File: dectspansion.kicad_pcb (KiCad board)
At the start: 4 copper layers, 37 x 36.6 mm, 19 parts, among them J1 Hexpansion-Connector, J2 Conn_01x03_Pin, J3 AudioJack4, U2 SC14CVMDECT

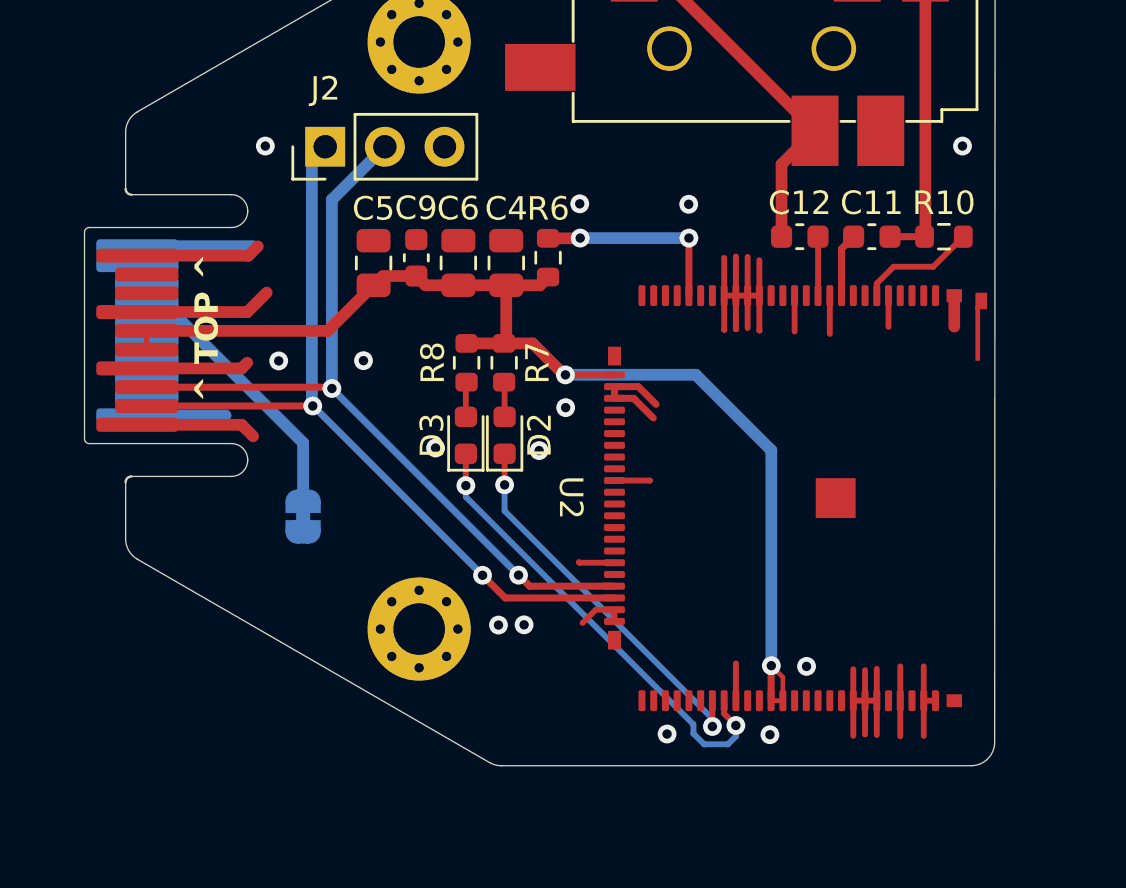
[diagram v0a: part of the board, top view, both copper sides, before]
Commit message: Adjustments to schmatic, board layout, and added part list to readme
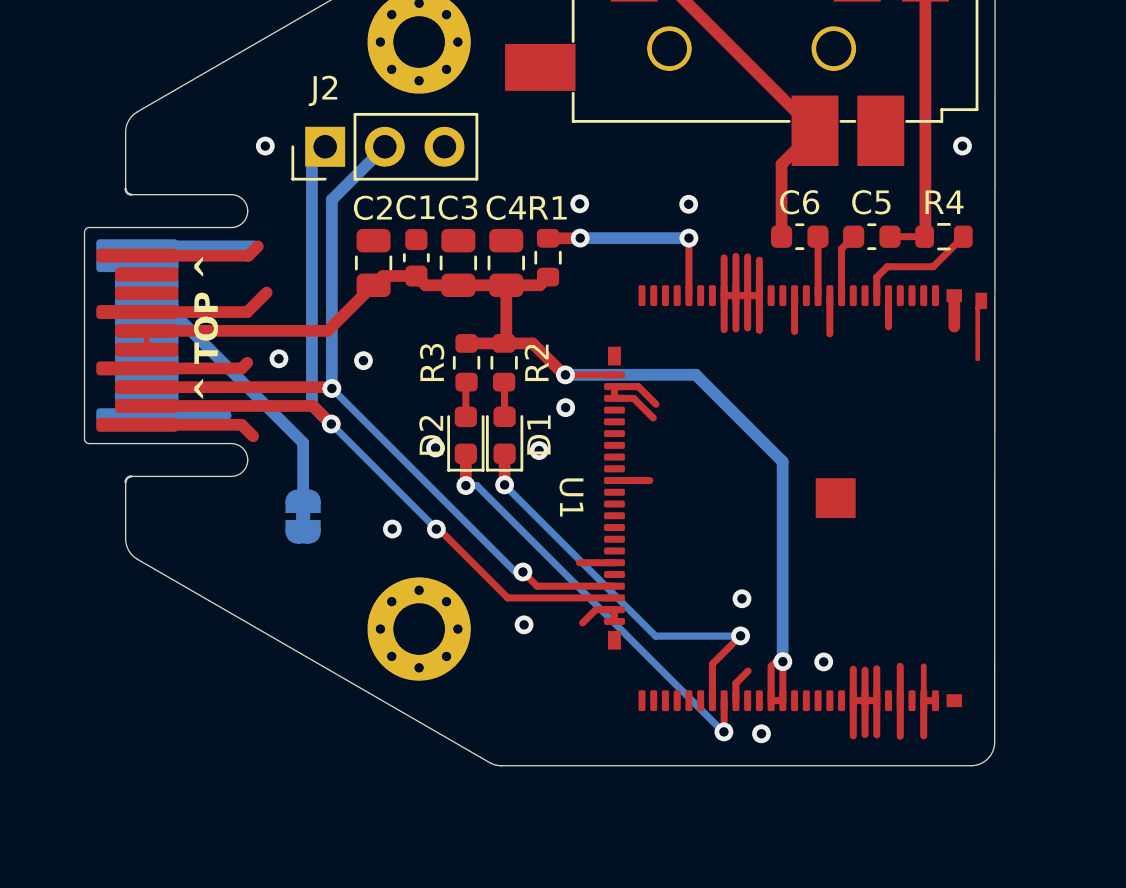
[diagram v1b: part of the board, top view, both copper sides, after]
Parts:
- C5: renamed from C11; value 0U1 -> 0u1
- C6: renamed from C12; value 1N -> 1n
- renumbered C9 to C1, C5 to C2, C6 to C3, D2 to D1, D3 to D2, R6 to R1, R7 to R2, R8 to R3, R10 to R4, U2 to U1
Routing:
- net /HS_I: track 34.6 -> 36.8 mm
- net Net-(D2-K): track 19.8 -> 18.0 mm
- net Net-(D1-K): track 16.8 -> 17.7 mm
- net +3V3: track 51.5 -> 52.1 mm

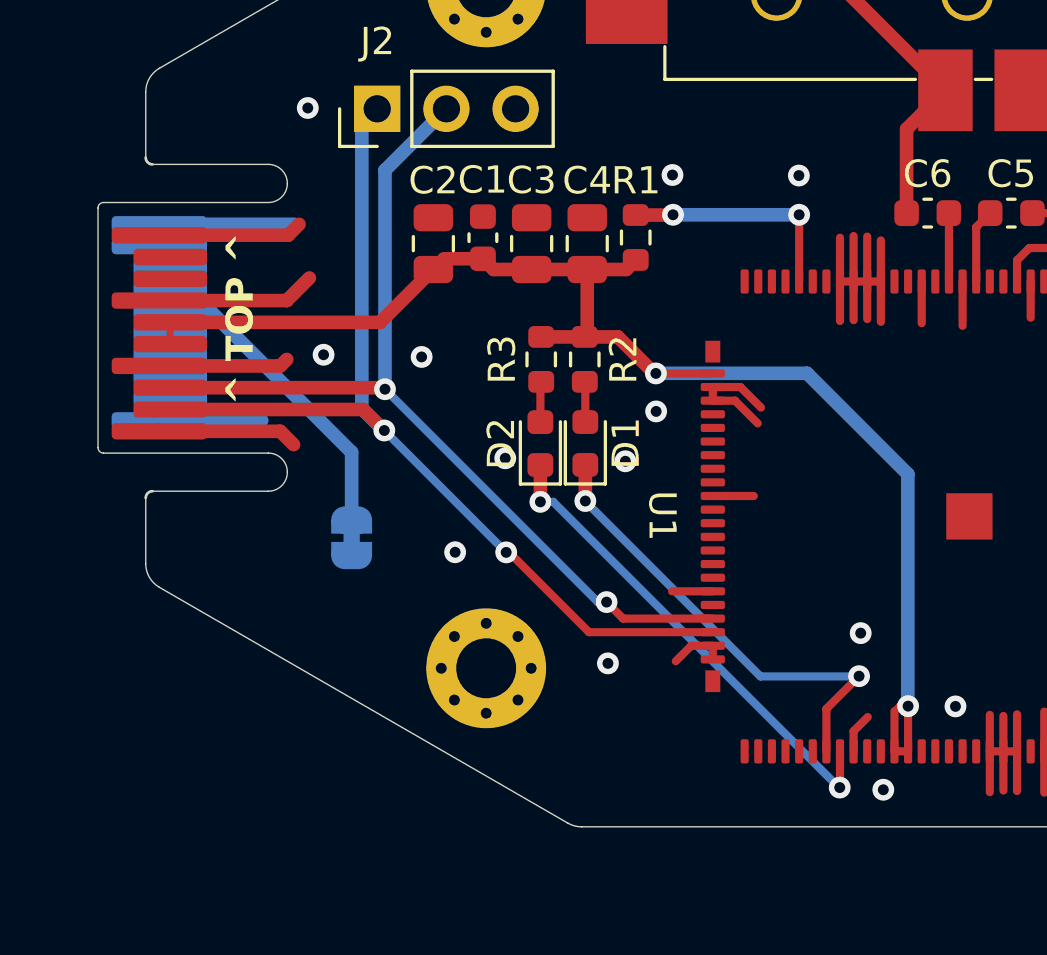
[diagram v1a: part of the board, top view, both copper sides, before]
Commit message: Added uart level shifting
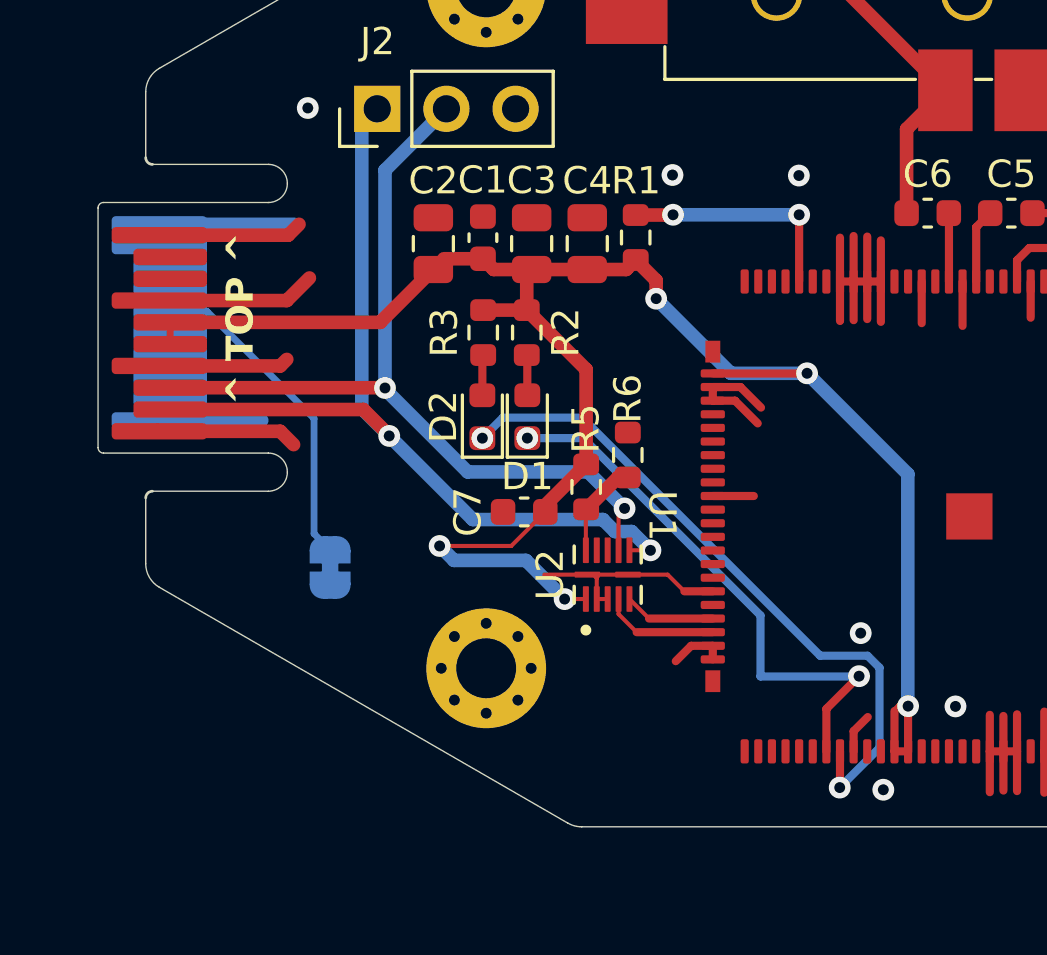
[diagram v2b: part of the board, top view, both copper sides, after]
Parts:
- added C7: 47p, Capacitor_SMD:C_0603_1608Metric, F.Cu at (113.9, 106.8)
- added R5: 1K, Resistor_SMD:R_0603_1608Metric, F.Cu at (116.2, 105.8)
- added R6: 1K, Resistor_SMD:R_0603_1608Metric, F.Cu at (117.7, 104.7)
- added U2: ~, 74AVC4T3144:74AVC4T3144, F.Cu at (117.0, 109.1)
- moved R2 2.35 mm to (114.0, 100.2)
- moved D1 2.35 mm to (114.0, 103.3)
- moved D2 2.35 mm to (112.4, 103.3)
- moved R3 2.35 mm to (112.4, 100.2)
- moved JP1 1.35 mm to (106.8, 108.8)
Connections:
- U1 pad 47: /HS_H -> Net-(U1-URX)
- U1 pad 48: /HS_I -> Net-(U1-UTX)
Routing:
- net +3V3: track 52.1 -> 71.7 mm, vias 2 -> 5
- net Net-(D2-K): track 18.0 -> 25.1 mm
- net GND: track 76.4 -> 82.7 mm, vias 14 -> 7
- net Net-(U1-UTX): track 0.00 -> 4.29 mm
- net /HS_H: track 35.2 -> 31.4 mm
- net /HS_I: track 36.8 -> 33.2 mm
- net Net-(U2-VCC(B)): track 0.00 -> 3.52 mm
- net Net-(U1-URX): track 0.00 -> 3.36 mm
- net Net-(D1-K): track 17.7 -> 20.4 mm
- net /HEXP_DET: track 11.4 -> 12.0 mm

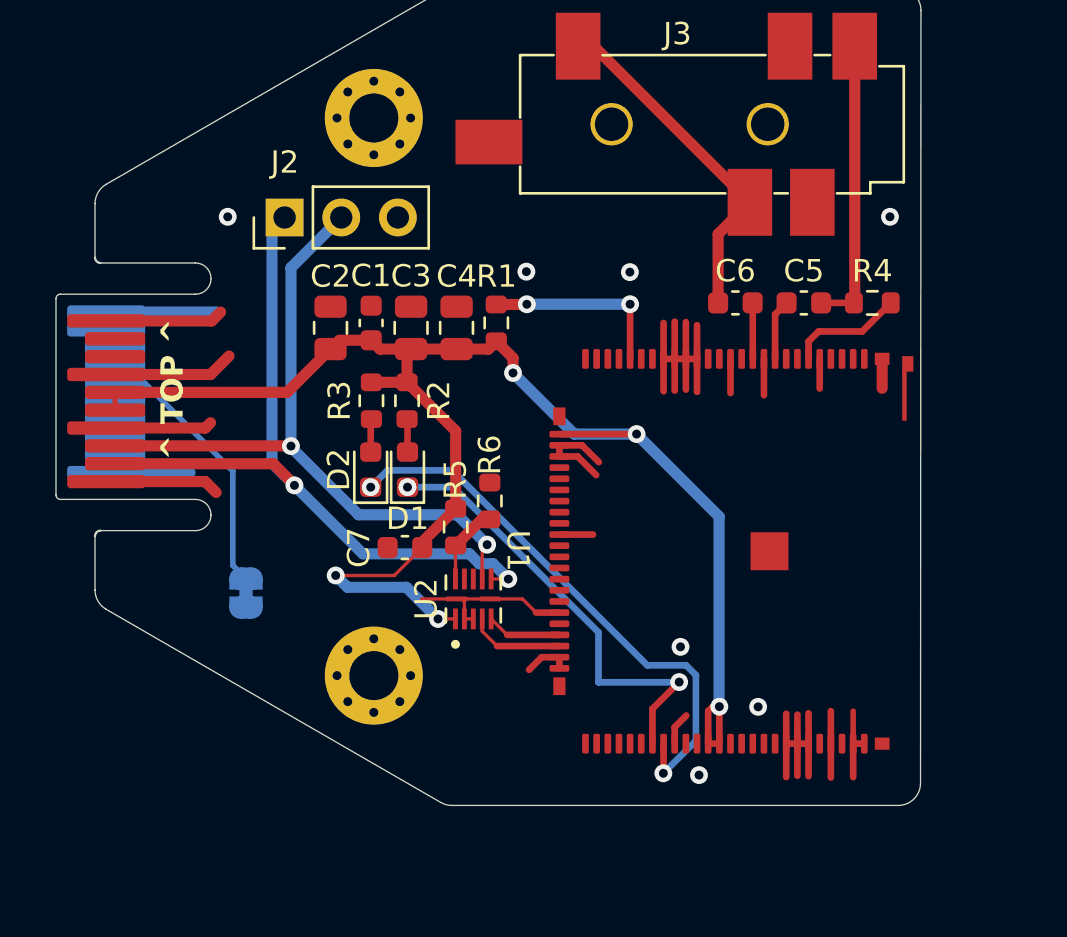
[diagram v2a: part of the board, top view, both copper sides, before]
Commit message: Added level shifitng, updated schematic, layout and gerbers
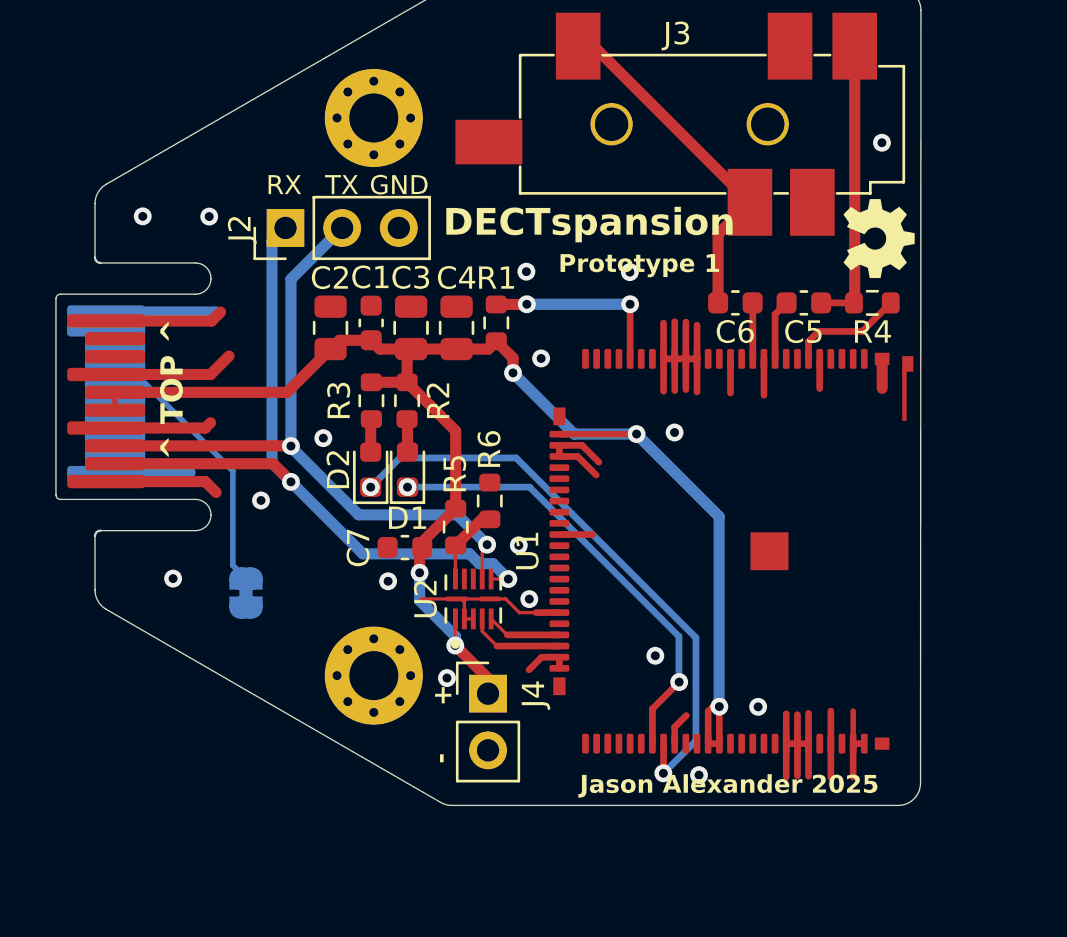
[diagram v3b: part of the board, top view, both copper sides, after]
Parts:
- added J4: Conn_01x02_Pin, Connector_PinHeader_2.54mm:PinHeader_1x02_P2.54mm_Vertical, F.Cu at (117.6, 113.3)
- moved J2 0.47 mm to (108.5, 92.4)
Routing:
- net +3V3: track 71.7 -> 70.2 mm
- net Net-(D2-K): track 25.1 -> 26.5 mm
- net /HS_I: track 33.2 -> 32.5 mm
- net GND: vias 7 -> 17
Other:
- board text added: "+"
- board text added: "-"
- board text added: "CERN Open Hardware Licence Version 2 - Strongly Reciprocal https://cern-ohl.web.cern.ch"
- board text added: "DECTspansion"
- board text added: "GND"
- board text added: "Jason Alexander 2025"
- board text added: "Prototype 1"
- board text added: "RX"
- board text added: "TX"
- board text added: "https://github.com/jasonalexander-ja/dectspansion"

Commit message: Fixed bug
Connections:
- R5 pad 1: Net-(U2-VCC(B)) -> Net-(U2-VCC(A))
- R6 pad 2: Net-(U2-VCC(B)) -> Net-(U2-VCC(A))
- U2 pad 1: +3V3 -> Net-(U2-VCC(A))
- U2 pad 11: Net-(U2-VCC(B)) -> +3V3
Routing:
- net Net-(U2-VCC(A)): track 0.00 -> 6.59 mm
- net Net-(U2-VCC(B)): track 3.52 -> 0.00 mm
- net GND: track 82.7 -> 81.1 mm
- net +3V3: track 70.2 -> 71.0 mm, vias 5 -> 6
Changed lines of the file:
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@@
 	(net 67 "unconnected-(U1-CIDINp-Pad65)")
 	(net 68 "unconnected-(U1-PAOUTn-Pad27)")
-	(net 69 "Net-(U2-VCC(B))")
+	(net 69 "Net-(U2-VCC(A))")
 	(net 70 "Net-(U1-URX)")
 	(net 71 "Net-(U1-UTX)")
@@
 			(layers "F.Cu" "F.Mask" "F.Paste")
 			(roundrect_rratio 0.25)
-			(net 69 "Net-(U2-VCC(B))")
+			(net 69 "Net-(U2-VCC(A))")
 			(pintype "passive")
 		)
@@
 			(layers "F.Cu" "F.Mask" "F.Paste")
 			(roundrect_rratio 0.25)
-			(net 69 "Net-(U2-VCC(B))")
+			(net 69 "Net-(U2-VCC(A))")
 			(pintype "passive")
 		)
@@
 			(layers "F.Cu" "F.Mask" "F.Paste")
 			(roundrect_rratio 0.125)
-			(net 1 "+3V3")
+			(net 69 "Net-(U2-VCC(A))")
 			(pinfunction "VCC(A)")
 			(pintype "power_in")
@@
 			(layers "F.Cu" "F.Mask" "F.Paste")
 			(roundrect_rratio 0.125)
-			(net 69 "Net-(U2-VCC(B))")
+			(net 1 "+3V3")
 			(pinfunction "VCC(B)")
 			(pintype "power_in")
@@
 	)
 	(segment
-		(start 116.15 109.9675)
-		(end 116.16 109.9575)
-		(width 0.15)
-		(layer "F.Cu")
-		(net 1)
-	)
-	(segment
 		(start 113.99 99.35)
 		(end 113.99 98.04)
@@
 	)
 	(segment
-		(start 114.67 106.916)
-		(end 114.67 106.76)
-		(width 0.5)
+		(start 124.275 101.675)
+		(end 124.28 101.67)
+		(width 0.3)
 		(layer "F.Cu")
 		(net 1)
 	)
 	(segment
-		(start 124.275 101.675)
-		(end 124.28 101.67)
-		(width 0.3)
+		(start 115.87 108.126686)
+		(end 115.901686 108.126686)
+		(width 0.15)
 		(layer "F.Cu")
 		(net 1)
@@
 	)
 	(segment
-		(start 116.15 111.15)
-		(end 117.62 112.62)
+		(start 117.22 111.84)
+		(end 117.62 112.24)
+		(width 0.5)
+		(layer "F.Cu")
+		(net 1)
+	)
+	(segment
+		(start 114.67 106.96)
+		(end 114.67 106.76)
 		(width 0.5)
 		(layer "F.Cu")
@@
 	)
 	(segment
-		(start 114.554 107.032)
-		(end 114.67 106.916)
-		(width 0.5)
-		(layer "F.Cu")
-		(net 1)
-	)
-	(segment
 		(start 118.74 98.26)
 		(end 117.99 97.51)
@@
 	)
 	(segment
-		(start 114.554 107.89)
-		(end 114.554 107.032)
+		(start 117.62 112.24)
+		(end 117.62 113.31)
 		(width 0.5)
 		(layer "F.Cu")
@@
 	)
 	(segment
-		(start 114.17 97.86)
-		(end 112.775 97.86)
-		(width 0.5)
+		(start 115.901686 108.126686)
+		(end 115.9425 108.1675)
+		(width 0.15)
 		(layer "F.Cu")
 		(net 1)
 	)
 	(segment
-		(start 116.15 111.15)
-		(end 116.15 109.9675)
+		(start 115.9425 108.1675)
+		(end 116.16 108.1675)
 		(width 0.15)
 		(layer "F.Cu")
@@
 	)
 	(segment
-		(start 117.62 112.62)
-		(end 117.62 113.31)
+		(start 114.17 97.86)
+		(end 112.775 97.86)
 		(width 0.5)
 		(layer "F.Cu")
@@
 	)
 	(via
-		(at 114.554 107.89)
+		(at 115.87 108.126686)
+		(size 0.8)
+		(drill 0.4)
+		(layers "F.Cu" "B.Cu")
+		(net 1)
+	)
+	(via
+		(at 114.67 106.96)
 		(size 0.8)
 		(drill 0.4)
@@
 	)
 	(via
-		(at 116.15 111.15)
+		(at 117.22 111.84)
 		(size 0.8)
 		(drill 0.4)
@@
 	)
 	(segment
+		(start 114.554 107.076)
+		(end 114.554 109.134)
+		(width 0.5)
+		(layer "B.Cu")
+		(net 1)
+	)
+	(segment
 		(start 121.48 101.67)
 		(end 118.74 98.93)
@@
 	)
 	(segment
-		(start 116.15 111.15)
-		(end 116.15 110.73)
+		(start 114.67 106.96)
+		(end 114.554 107.076)
 		(width 0.5)
 		(layer "B.Cu")
@@
 	)
 	(segment
+		(start 114.554 109.134)
+		(end 116.15 110.73)
+		(width 0.5)
+		(layer "B.Cu")
+		(net 1)
+	)
+	(segment
 		(start 116.15 110.73)
-		(end 114.554 109.134)
+		(end 116.15 110.77)
+		(width 0.5)
+		(layer "B.Cu")
+		(net 1)
+	)
+	(segment
+		(start 115.756686 108.126686)
+		(end 115.87 108.126686)
 		(width 0.5)
 		(layer "B.Cu")
@@
 	)
 	(segment
-		(start 114.554 109.134)
-		(end 114.554 107.89)
+		(start 114.67 106.96)
+		(end 114.67 107.04)
 		(width 0.5)
 		(layer "B.Cu")
@@
 	)
 	(segment
+		(start 114.67 107.04)
+		(end 115.756686 108.126686)
+		(width 0.5)
+		(layer "B.Cu")
+		(net 1)
+	)
+	(segment
+		(start 116.15 110.77)
+		(end 117.22 111.84)
+		(width 0.5)
+		(layer "B.Cu")
+		(net 1)
+	)
+	(segment
 		(start 125.99 115.55)
 		(end 125.99 114.81)
@@
 	)
 	(segment
-		(start 116.215 109.0625)
-		(end 114.6325 109.0625)
-		(width 0.15)
-		(layer "F.Cu")
-		(net 2)
-	)
-	(segment
 		(start 131.49 115.55)
 		(end 131.49 114.25)
@@
 	)
 	(via
-		(at 115.78 112.61)
+		(at 115.73 111.83)
 		(size 0.8)
 		(drill 0.4)
@@
 	)
 	(segment
-		(start 117.841 107.481)
-		(end 118.53 108.17)
+		(start 111.08 106.11)
+		(end 115.856504 106.11)
 		(width 0.5)
 		(layer "B.Cu")
@@
 	)
 	(segment
-		(start 107.934 93.036)
-		(end 108.54 92.43)
+		(start 115.856504 106.11)
+		(end 117.227504 107.481)
 		(width 0.5)
 		(layer "B.Cu")
@@
 	)
 	(segment
-		(start 116.786504 107.04)
-		(end 117.227504 107.481)
+		(start 108.784 103.814)
+		(end 111.08 106.11)
+		(width 0.5)
+		(layer "B.Cu")
+		(net 12)
+	)
+	(segment
+		(start 107.934 93.036)
+		(end 108.54 92.43)
 		(width 0.5)
 		(layer "B.Cu")
@@
 	)
 	(segment
-		(start 112.01 107.04)
-		(end 116.786504 107.04)
-		(width 0.5)
-		(layer "B.Cu")
-		(net 12)
-	)
-	(segment
-		(start 108.784 103.814)
-		(end 112.01 107.04)
+		(start 117.841 107.481)
+		(end 118.53 108.17)
 		(width 0.5)
 		(layer "B.Cu")
@@
 	)
 	(segment
-		(start 116.16 108.1675)
-		(end 116.16 106.675)
+		(start 116.15 109.9675)
+		(end 116.16 109.9575)
 		(width 0.15)
 		(layer "F.Cu")
@@
 	)
 	(segment
-		(start 116.16 106.675)
-		(end 116.17 106.665)
-		(width 0.15)
+		(start 115.04 109.4)
+		(end 115.04 107.79)
+		(width 0.3)
 		(layer "F.Cu")
 		(net 69)
@@
 	)
 	(segment
+		(start 115.04 109.4)
+		(end 115.5975 109.9575)
+		(width 0.15)
+		(layer "F.Cu")
+		(net 69)
+	)
+	(segment
+		(start 116.165 106.665)
+		(end 116.17 106.665)
+		(width 0.3)
+		(layer "F.Cu")
+		(net 69)
+	)
+	(segment
+		(start 115.04 107.79)
+		(end 116.165 106.665)
+		(width 0.3)
+		(layer "F.Cu")
+		(net 69)
+	)
+	(segment
 		(start 117.34 105.495)
 		(end 117.7 105.495)
@@
 		(layer "F.Cu")
 		(net 69)
+	)
+	(segment
+		(start 115.5975 109.9575)
+		(end 116.16 109.9575)
+		(width 0.15)
+		(layer "F.Cu")
+		(net 69)
